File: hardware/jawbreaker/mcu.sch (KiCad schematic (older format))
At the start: 114 parts, among them J1 GSG-USB-MICRO-B, P1 ANALOG, P10 BANK1_AUX, P11 SPIFI, P12 SD, P13 ADC/DAC, P14 LPC_ISP, P15 I2S, P16 1V8, P17 VCC, P18 CPLD_JTAG, P19 BOOT1, P2 LPC_JTAG, P20 BOOT2, P21 BOOT3, P22 BANK1_PWR, P3 LPC_MISC, P4 BOOT0, P5 GPIO, P6 CLOCK_CTL, P7 XCVR_CTL, P8 BANK2_AUX, P9 SPI, U1 GSG-IP4220CZ6, U2 LPC43XXFBD144, U3 W25Q80BV, U4 GSG-XC2C64A-7VQG100C, U5 TPS62410

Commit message: dedicated crystal for mcu. also GP_CLKIN from clock generator as an option
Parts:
- added C? (x2): 10pF, symbol C
- added X?: MCU_XTAL, symbol GSG-XTAL4PIN
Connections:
- net GND: now also C?.2, C?.2, X?.2, X?.4
- net XTAL1: now also C?.1, X?.1; no longer C16.2, C18.2
- net XTAL2: now reaches U2.13 (XTAL2)
- net XTAL2: now also C?.1, X?.3
- net GP_CLKIN: now reaches U2.14 (P4_7)
- net GP_CLKIN: now also C16.2, C18.2
- no-connect marks 32 -> 30
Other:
- moved on the sheet: P10, P7, P8

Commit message: changed boot jumper headers to resistors
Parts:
- removed P19: BOOT1, symbol CONN_3
- removed P20: BOOT2, symbol CONN_3
- removed P21: BOOT3, symbol CONN_3
- removed P4: BOOT0, symbol CONN_3
- added R? (x4): DNP, symbol R
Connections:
- net BOOT0: now also R?.2
- net BOOT1: now also R41.2, R?.1; no longer R41.1
- net BOOT2: now also R42.2, R?.1; no longer R42.1
- net BOOT3: now also R43.2, R?.1; no longer R43.1
- net GND: now also R41.1, R42.1, R43.1, R?.1
- net VCC: now also R4.2, R?.2, R?.2, R?.2
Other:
- moved on the sheet: C?, R4, R41, R42, R43, X?

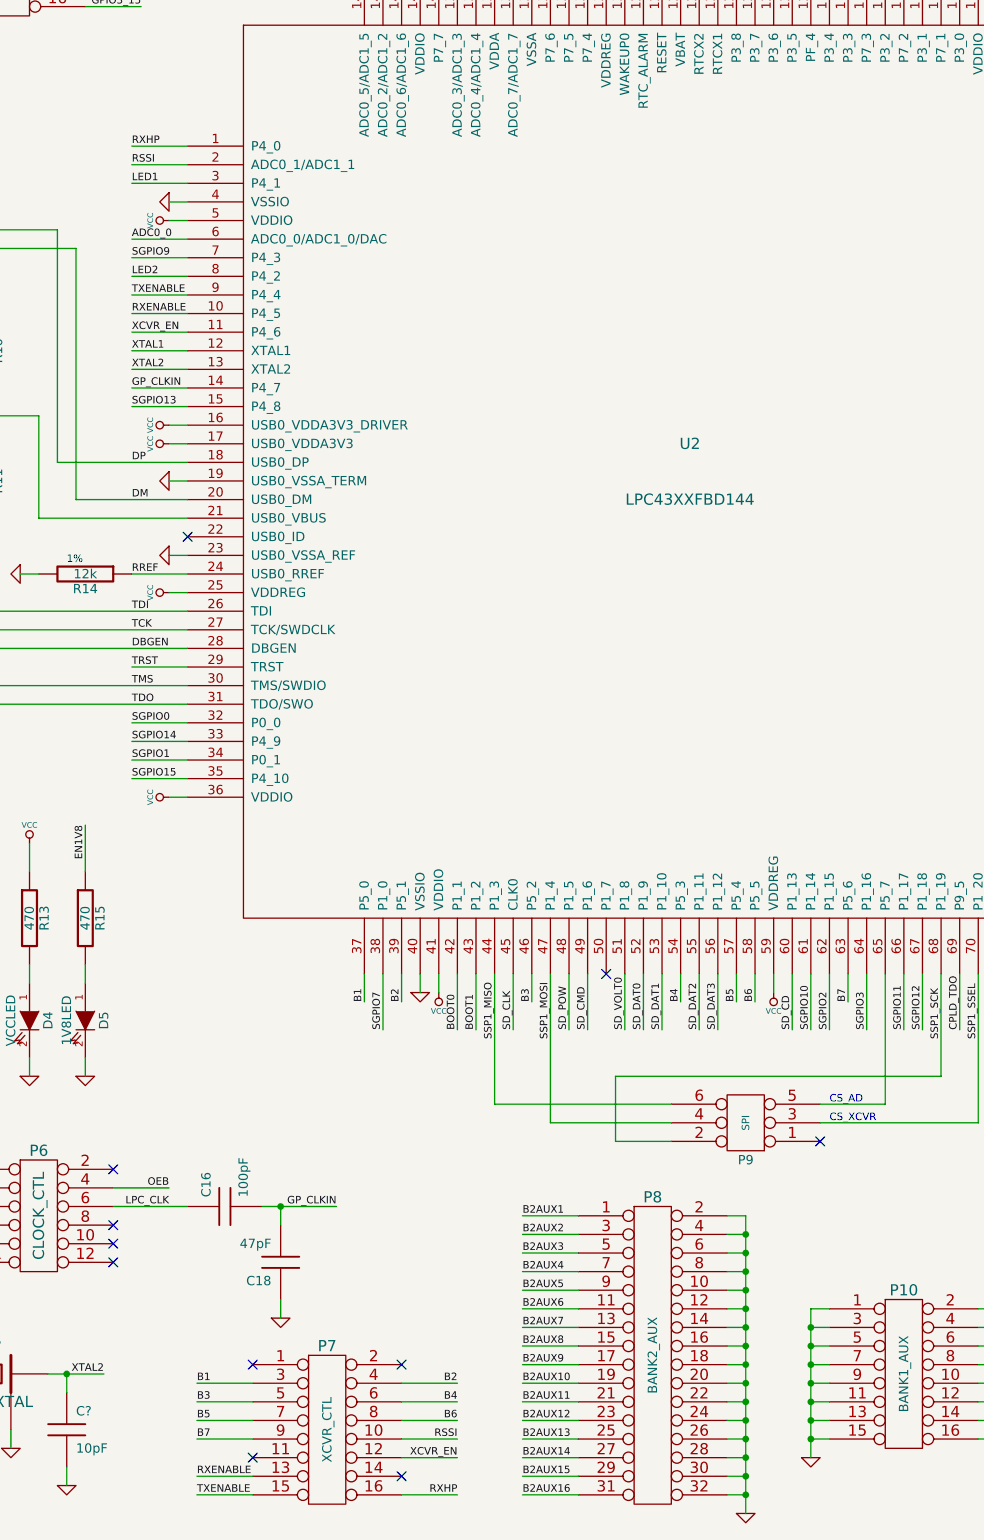
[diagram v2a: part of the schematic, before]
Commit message: removed XCVR_CTL signals that we never used
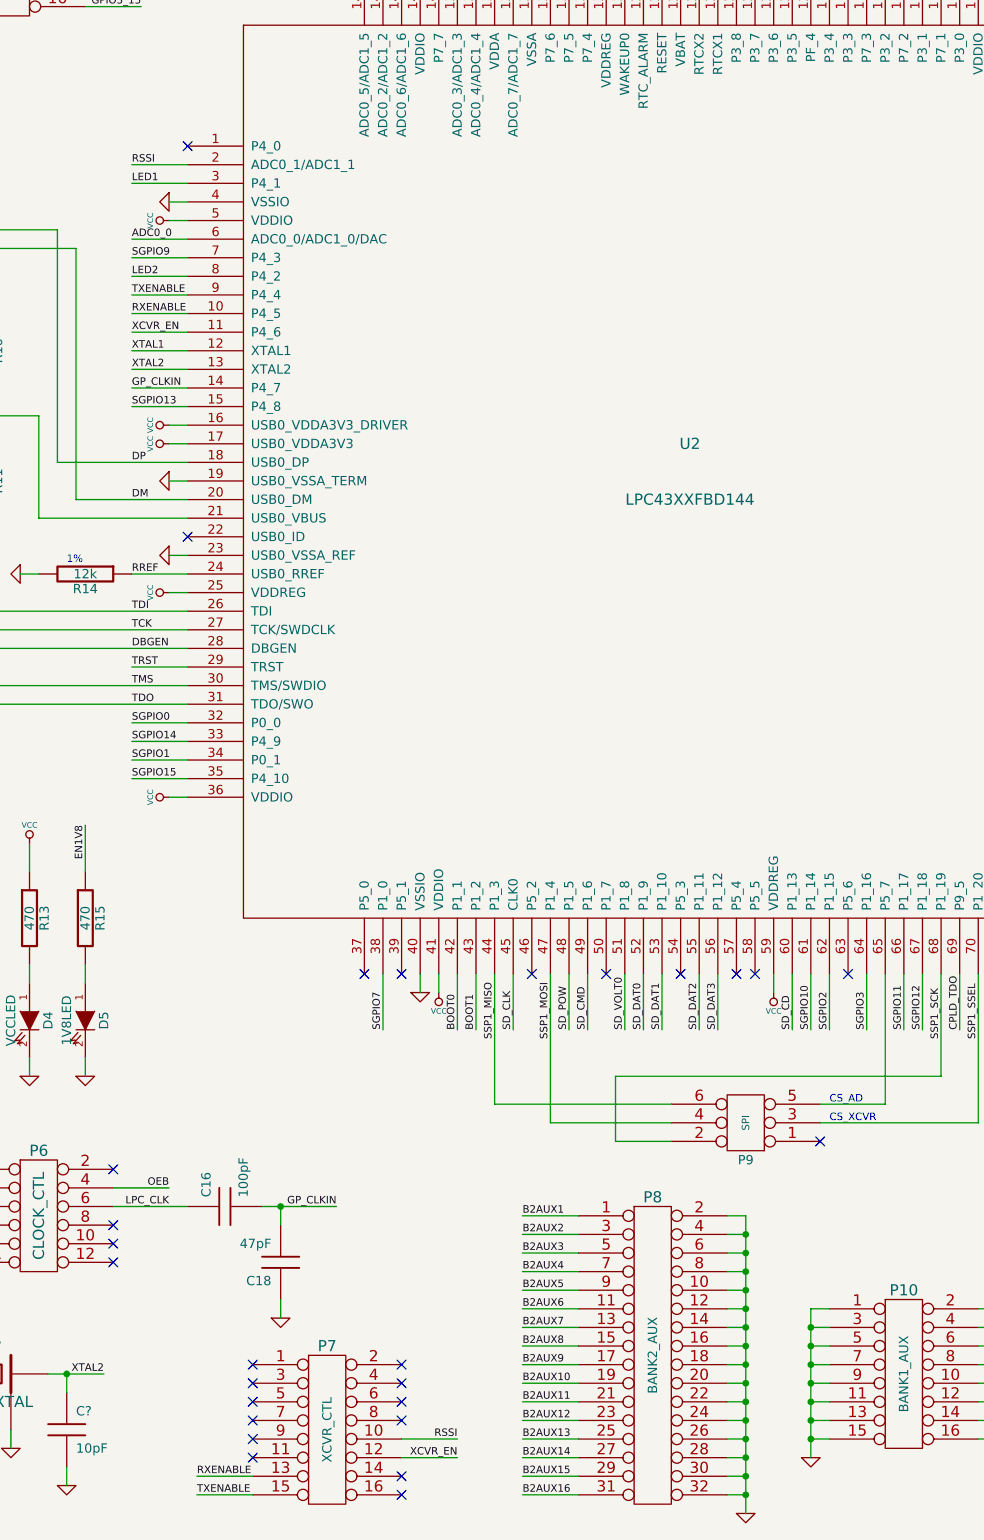
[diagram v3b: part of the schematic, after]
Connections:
- net B1: no longer names the net of U2.37 (P5_0)
- net B1: no longer P7.3
- net B2: no longer names the net of U2.39 (P5_1)
- net B2: no longer P7.4
- net B3: no longer names the net of U2.46 (P5_2)
- net B3: no longer P7.5
- net B4: no longer names the net of U2.54 (P5_3)
- net B4: no longer P7.6
- net B5: no longer names the net of U2.57 (P5_4)
- net B5: no longer P7.7
- net B6: no longer names the net of U2.58 (P5_5)
- net B6: no longer P7.8
- net B7: no longer names the net of U2.63 (P5_6)
- net B7: no longer P7.9
- net RXHP: no longer names the net of U2.1 (P4_0)
- net RXHP: no longer P7.16
- no-connect marks 30 -> 46
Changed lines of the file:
@@
-EESchema Schematic File Version 2  date Thu Aug 23 23:42:08 2012
+EESchema Schematic File Version 2  date Thu Aug 23 23:50:26 2012
 LIBS:power
 LIBS:device
@@
 Comment4 ""
 $EndDescr
-Text Label 2300 9300 2    40   ~ 0
-BOOT3
-$Comp
-L VCC #PWR?
-U 1 1 503713EC
-P 2050 8600
-F 0 "#PWR?" H 2050 8700 30  0001 C CNN
-F 1 "VCC" H 2050 8700 30  0000 C CNN
-	1    2050 8600
-	1    0    0    -1
-$EndComp
-$Comp
-L R R?
-U 1 1 503713EB
-P 2050 8950
-F 0 "R?" V 2130 8950 50  0000 C CNN
-F 1 "DNP" V 2050 8950 50  0000 C CNN
-F 4 "Panasonic" H 2050 8950 60  0001 C CNN "Manufacturer"
-F 5 "ERJ-3GEYJ103V" H 2050 8950 60  0001 C CNN "Part Number"
-F 6 "RES 10K OHM 1/10W 5% 0603 SMD" H 2050 8950 60  0001 C CNN "Description"
-	1    2050 8950
-	-1   0    0    1
-$EndComp
-$Comp
-L GND #PWR?
-U 1 1 503713EA
-P 2050 10000
-F 0 "#PWR?" H 2050 10000 30  0001 C CNN
-F 1 "GND" H 2050 9930 30  0001 C CNN
-	1    2050 10000
-	1    0    0    -1
-$EndComp
+NoConn ~ 7850 7450
+NoConn ~ 7350 7450
+NoConn ~ 7250 7450
+NoConn ~ 6950 7450
+NoConn ~ 6150 7450
+NoConn ~ 5450 7450
+NoConn ~ 5250 7450
 Wire Wire Line
 	2050 10000 2050 9900
@@
 Wire Wire Line
 	1600 10000 1600 9900
-$Comp
-L GND #PWR?
-U 1 1 503713B9
-P 1600 10000
-F 0 "#PWR?" H 1600 10000 30  0001 C CNN
-F 1 "GND" H 1600 9930 30  0001 C CNN
-	1    1600 10000
-	1    0    0    -1
-$EndComp
-$Comp
-L R R?
-U 1 1 503713B8
-P 1600 8950
-F 0 "R?" V 1680 8950 50  0000 C CNN
-F 1 "DNP" V 1600 8950 50  0000 C CNN
-F 4 "Panasonic" H 1600 8950 60  0001 C CNN "Manufacturer"
-F 5 "ERJ-3GEYJ103V" H 1600 8950 60  0001 C CNN "Part Number"
-F 6 "RES 10K OHM 1/10W 5% 0603 SMD" H 1600 8950 60  0001 C CNN "Description"
-	1    1600 8950
-	-1   0    0    1
-$EndComp
-$Comp
-L VCC #PWR?
-U 1 1 503713B7
-P 1600 8600
-F 0 "#PWR?" H 1600 8700 30  0001 C CNN
-F 1 "VCC" H 1600 8700 30  0000 C CNN
-	1    1600 8600
-	1    0    0    -1
-$EndComp
-Text Label 1850 9300 2    40   ~ 0
-BOOT2
-Text Label 1400 9300 2    40   ~ 0
-BOOT1
-$Comp
-L VCC #PWR?
-U 1 1 50371392
-P 1150 8600
-F 0 "#PWR?" H 1150 8700 30  0001 C CNN
-F 1 "VCC" H 1150 8700 30  0000 C CNN
-	1    1150 8600
-	1    0    0    -1
-$EndComp
-$Comp
-L R R?
-U 1 1 50371390
-P 1150 8950
-F 0 "R?" V 1230 8950 50  0000 C CNN
-F 1 "DNP" V 1150 8950 50  0000 C CNN
-F 4 "Panasonic" H 1150 8950 60  0001 C CNN "Manufacturer"
-F 5 "ERJ-3GEYJ103V" H 1150 8950 60  0001 C CNN "Part Number"
-F 6 "RES 10K OHM 1/10W 5% 0603 SMD" H 1150 8950 60  0001 C CNN "Description"
-	1    1150 8950
-	-1   0    0    1
-$EndComp
-$Comp
-L GND #PWR?
-U 1 1 5037138F
-P 1150 10000
-F 0 "#PWR?" H 1150 10000 30  0001 C CNN
-F 1 "GND" H 1150 9930 30  0001 C CNN
-	1    1150 10000
-	1    0    0    -1
-$EndComp
 Wire Wire Line
 	1150 10000 1150 9900
@@
 	5450 9950 5750 9950
 Wire Wire Line
-	5450 9750 5750 9750
-Wire Wire Line
 	4650 10250 4350 10250
 Wire Wire Line
-	4650 9850 4350 9850
-Wire Wire Line
-	4650 9650 4350 9650
-Wire Wire Line
-	7350 7450 7350 7600
-Wire Wire Line
-	6950 7450 6950 7600
-Wire Wire Line
-	6150 7450 6150 7600
-Wire Wire Line
-	5250 7450 5250 7600
-Wire Wire Line
 	16150 2250 16150 2150
 Wire Wire Line
@@
 	16150 1650 16150 1550
 Wire Wire Line
-	5450 7450 5450 7600
-Wire Wire Line
-	7250 7450 7250 7600
-Wire Wire Line
-	7850 7450 7850 7600
-Wire Wire Line
-	4650 9750 4350 9750
-Wire Wire Line
-	4650 9950 4350 9950
-Wire Wire Line
 	4650 10150 4350 10150
 Wire Wire Line
-	5450 9650 5750 9650
-Wire Wire Line
-	5450 9850 5750 9850
-Wire Wire Line
 	5450 10050 5750 10050
 Wire Wire Line
-	5450 10250 5750 10250
-Wire Wire Line
 	4300 3900 4000 3900
 Wire Wire Line
-	4300 3000 4000 3000
-Wire Wire Line
 	3100 8700 2900 8700
 Wire Wire Line
@@
 Wire Wire Line
 	700  10000 700  9900
+NoConn ~ 4300 3000
+NoConn ~ 5450 10250
+NoConn ~ 5450 9850
+NoConn ~ 5450 9750
+NoConn ~ 5450 9650
+NoConn ~ 4650 9950
+NoConn ~ 4650 9850
+NoConn ~ 4650 9750
+NoConn ~ 4650 9650
+Text Label 2300 9300 2    40   ~ 0
+BOOT3
+$Comp
+L VCC #PWR?
+U 1 1 503713EC
+P 2050 8600
+F 0 "#PWR?" H 2050 8700 30  0001 C CNN
+F 1 "VCC" H 2050 8700 30  0000 C CNN
+	1    2050 8600
+	1    0    0    -1
+$EndComp
+$Comp
+L R R?
+U 1 1 503713EB
+P 2050 8950
+F 0 "R?" V 2130 8950 50  0000 C CNN
+F 1 "DNP" V 2050 8950 50  0000 C CNN
+F 4 "Panasonic" H 2050 8950 60  0001 C CNN "Manufacturer"
+F 5 "ERJ-3GEYJ103V" H 2050 8950 60  0001 C CNN "Part Number"
+F 6 "RES 10K OHM 1/10W 5% 0603 SMD" H 2050 8950 60  0001 C CNN "Description"
+	1    2050 8950
+	-1   0    0    1
+$EndComp
+$Comp
+L GND #PWR?
+U 1 1 503713EA
+P 2050 10000
+F 0 "#PWR?" H 2050 10000 30  0001 C CNN
+F 1 "GND" H 2050 9930 30  0001 C CNN
+	1    2050 10000
+	1    0    0    -1
+$EndComp
+$Comp
+L GND #PWR?
+U 1 1 503713B9
+P 1600 10000
+F 0 "#PWR?" H 1600 10000 30  0001 C CNN
+F 1 "GND" H 1600 9930 30  0001 C CNN
+	1    1600 10000
+	1    0    0    -1
+$EndComp
+$Comp
+L R R?
+U 1 1 503713B8
+P 1600 8950
+F 0 "R?" V 1680 8950 50  0000 C CNN
+F 1 "DNP" V 1600 8950 50  0000 C CNN
+F 4 "Panasonic" H 1600 8950 60  0001 C CNN "Manufacturer"
+F 5 "ERJ-3GEYJ103V" H 1600 8950 60  0001 C CNN "Part Number"
+F 6 "RES 10K OHM 1/10W 5% 0603 SMD" H 1600 8950 60  0001 C CNN "Description"
+	1    1600 8950
+	-1   0    0    1
+$EndComp
+$Comp
+L VCC #PWR?
+U 1 1 503713B7
+P 1600 8600
+F 0 "#PWR?" H 1600 8700 30  0001 C CNN
+F 1 "VCC" H 1600 8700 30  0000 C CNN
+	1    1600 8600
+	1    0    0    -1
+$EndComp
+Text Label 1850 9300 2    40   ~ 0
+BOOT2
+Text Label 1400 9300 2    40   ~ 0
+BOOT1
+$Comp
+L VCC #PWR?
+U 1 1 50371392
+P 1150 8600
+F 0 "#PWR?" H 1150 8700 30  0001 C CNN
+F 1 "VCC" H 1150 8700 30  0000 C CNN
+	1    1150 8600
+	1    0    0    -1
+$EndComp
+$Comp
+L R R?
+U 1 1 50371390
+P 1150 8950
+F 0 "R?" V 1230 8950 50  0000 C CNN
+F 1 "DNP" V 1150 8950 50  0000 C CNN
+F 4 "Panasonic" H 1150 8950 60  0001 C CNN "Manufacturer"
+F 5 "ERJ-3GEYJ103V" H 1150 8950 60  0001 C CNN "Part Number"
+F 6 "RES 10K OHM 1/10W 5% 0603 SMD" H 1150 8950 60  0001 C CNN "Description"
+	1    1150 8950
+	-1   0    0    1
+$EndComp
+$Comp
+L GND #PWR?
+U 1 1 5037138F
+P 1150 10000
+F 0 "#PWR?" H 1150 10000 30  0001 C CNN
+F 1 "GND" H 1150 9930 30  0001 C CNN
+	1    1150 10000
+	1    0    0    -1
+$EndComp
 $Comp
 L GND #PWR?
@@
 	1    0    0    -1
 $EndComp
-Text Label 4000 3000 0    40   ~ 0
-RXHP
 Text Label 4000 3800 0    40   ~ 0
 TXENABLE
@@
 NoConn ~ 4650 10050
 NoConn ~ 5450 10150
-Text Label 5750 10250 2    40   ~ 0
-RXHP
 Text Label 5750 10050 2    40   ~ 0
 XCVR_EN
 Text Label 5750 9950 2    40   ~ 0
 RSSI
-Text Label 5750 9850 2    40   ~ 0
-B6
-Text Label 4350 9950 0    40   ~ 0
-B7
-Text Label 4350 9850 0    40   ~ 0
-B5
-Text Label 4350 9750 0    40   ~ 0
-B3
-Text Label 5750 9750 2    40   ~ 0
-B4
-Text Label 5750 9650 2    40   ~ 0
-B2
-Text Label 4350 9650 0    40   ~ 0
-B1
 Text Label 4350 10150 0    40   ~ 0
 RXENABLE
@@
 	1    0    0    -1
 $EndComp
-Text Label 7850 7600 1    40   ~ 0
-B7
-Text Label 7350 7600 1    40   ~ 0
-B6
-Text Label 7250 7600 1    40   ~ 0
-B5
-Text Label 6950 7600 1    40   ~ 0
-B4
-Text Label 6150 7600 1    40   ~ 0
-B3
-Text Label 5450 7600 1    40   ~ 0
-B2
 NoConn ~ 6550 7450
-Text Label 5250 7600 1    40   ~ 0
-B1
 Text Notes 7750 8150 0    40   ~ 0
 CS_AD

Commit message: changed bank1 power header to resistors, wired spifi header (cut traces to use header)
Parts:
- removed P22: BANK1_PWR, symbol CONN_3
- added R?: DNP, symbol R
- added R?: 10k, symbol R
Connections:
- net +1.8V: now also R?.2
- net SPIFI_CS: now also P11.7 (P7), U3.1 (CS)
- net SPIFI_MISO: now also P11.1 (P1), U3.2 (DO)
- net SPIFI_MOSI: now also P11.3 (P3), U3.5 (DI)
- net SPIFI_SCK: now also P11.5 (P5), U3.6 (CLK)
- net SPIFI_SIO2: now also P11.11, U3.3 (WP)
- net SPIFI_SIO3: now also P11.9, U3.7 (HOLD)
- net VCC: now also R?.2
- net VCCIO1: now also R?.1, R?.1

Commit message: global labels for DA* and DD*, 39 ohm series resistors
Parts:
- removed P13: ADC/DAC, symbol CONN_20X2
- removed R19, R20, R21, R22, R23, R24, R25, R26, R27: 100, symbol R
- added R? (x17): 39, symbol R
- R18: value 100 -> 39; Description RES 100 OHM 1/10W 5% 0603 SMD -> (none); Manufacturer Panasonic -> (none); Part Number ERJ-3GEYJ101V -> (none)
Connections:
- net DA0: now also R?.2; no longer U4.43 (BANK1F4M8)
- net DA1: now also R?.2; no longer U4.42 (BANK1F4M7)
- net DA2: now also R?.2; no longer U4.41 (BANK1F4M6)
- net DA3: now also R?.2; no longer U4.40 (BANK1F4M5)
- net DA4: now also R?.2; no longer U4.39 (BANK1F4M4)
- net DA5: now also R?.2; no longer U4.37 (BANK1F4M3)
- net DA6: now also R?.2; no longer U4.36 (BANK1F4M2)
- net DA7: now also R?.2; no longer U4.35 (BANK1F4M1)
- net DD0: now also R?.2; no longer U4.34 (BANK1F2M16)
- net DD1: now also R?.2; no longer U4.33 (BANK1F2M15)
- net DD2: now also R?.2; no longer U4.32 (BANK1F2M14)
- net DD3: now also R?.2; no longer U4.30 (BANK1F2M13)
- net DD4: now also R?.2; no longer U4.29 (BANK1F2M12)
- net DD5: now also R?.2; no longer U4.28 (BANK1F2M11)
- net DD6: now also R?.2; no longer U4.24 (BANK1F2M9)
- net DD7: now also R?.2; no longer U4.19 (BANK1F2M6)
- net DD8: now also R?.2; no longer U4.18 (BANK1F2M5)
- net DD9: now also R18.2; no longer R18.1, U4.17 (BANK1F2M4)
- new net BANK1F2M11: R?.1, U4.28 (BANK1F2M11)
- new net BANK1F2M12: R?.1, U4.29 (BANK1F2M12)
- new net BANK1F2M13: R?.1, U4.30 (BANK1F2M13)
- new net BANK1F2M14: R?.1, U4.32 (BANK1F2M14)
- new net BANK1F2M15: R?.1, U4.33 (BANK1F2M15)
- new net BANK1F2M16: R?.1, U4.34 (BANK1F2M16)
- new net BANK1F2M4: R18.1, U4.17 (BANK1F2M4)
- new net BANK1F2M5: R?.1, U4.18 (BANK1F2M5)
- new net BANK1F2M6: R?.1, U4.19 (BANK1F2M6)
- new net BANK1F2M9: R?.1, U4.24 (BANK1F2M9)
- new net BANK1F4M1: R?.1, U4.35 (BANK1F4M1)
- new net BANK1F4M2: R?.1, U4.36 (BANK1F4M2)
- new net BANK1F4M3: R?.1, U4.37 (BANK1F4M3)
- new net BANK1F4M4: R?.1, U4.39 (BANK1F4M4)
- new net BANK1F4M5: R?.1, U4.40 (BANK1F4M5)
- new net BANK1F4M6: R?.1, U4.41 (BANK1F4M6)
- new net BANK1F4M7: R?.1, U4.42 (BANK1F4M7)
- new net BANK1F4M8: R?.1, U4.43 (BANK1F4M8)
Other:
- moved on the sheet: R18

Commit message: global labels for xcvr control
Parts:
- removed P7: XCVR_CTL, symbol CONN_8X2
- P11: Note (none) -> DNP
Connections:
- no-connect marks 46 -> 34
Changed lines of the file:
@@
-EESchema Schematic File Version 2  date Fri Aug 24 00:37:44 2012
+EESchema Schematic File Version 2  date Fri Aug 24 09:40:20 2012
 LIBS:power
 LIBS:device
@@
 Comment4 ""
 $EndDescr
+Text GLabel 4200 4000 0    40   Input ~ 0
+XCVR_EN
+Text GLabel 4200 3900 0    40   Input ~ 0
+RXENABLE
+Text GLabel 4200 3800 0    40   Input ~ 0
+TXENABLE
+Text GLabel 4200 3100 0    40   Input ~ 0
+RSSI
 Text GLabel 11400 7850 0    40   Input ~ 0
 GCK0
@@
 	8350 2050 8350 1750
 Wire Wire Line
-	4300 3100 4000 3100
+	4300 3100 4200 3100
 Wire Wire Line
 	9550 7400 9900 7400
@@
 	3100 8600 2900 8600
 Wire Wire Line
-	4300 3800 4000 3800
-Wire Wire Line
-	4300 4000 4000 4000
+	4300 3800 4200 3800
 Wire Wire Line
-	5450 9950 5750 9950
-Wire Wire Line
-	4650 10250 4350 10250
+	4300 4000 4200 4000
 Wire Wire Line
 	16150 2250 16150 2150
@@
 	16150 1650 16150 1550
 Wire Wire Line
-	4650 10150 4350 10150
-Wire Wire Line
-	5450 10050 5750 10050
-Wire Wire Line
-	4300 3900 4000 3900
+	4300 3900 4200 3900
 Wire Wire Line
 	3100 8700 2900 8700
@@
 NoConn ~ 5250 7450
 NoConn ~ 4300 3000
-NoConn ~ 5450 10250
-NoConn ~ 5450 9850
-NoConn ~ 5450 9750
-NoConn ~ 5450 9650
-NoConn ~ 4650 9950
-NoConn ~ 4650 9850
-NoConn ~ 4650 9750
-NoConn ~ 4650 9650
 Text Label 2300 9300 2    40   ~ 0
 BOOT3
@@
 Text Label 8650 1750 3    40   ~ 0
 GPIO3_8
-Text Label 4000 3100 0    40   ~ 0
-RSSI
 $Comp
 L VCC #PWR026
@@
 	1    0    0    -1
 $EndComp
-Text Label 4000 3800 0    40   ~ 0
-TXENABLE
-Text Label 4000 3900 0    40   ~ 0
-RXENABLE
-Text Label 4000 4000 0    40   ~ 0
-XCVR_EN
-NoConn ~ 4650 9550
-NoConn ~ 5450 9550
-NoConn ~ 4650 10050
-NoConn ~ 5450 10150
-Text Label 5750 10050 2    40   ~ 0
-XCVR_EN
-Text Label 5750 9950 2    40   ~ 0
-RSSI
-Text Label 4350 10150 0    40   ~ 0
-RXENABLE
-Text Label 4350 10250 0    40   ~ 0
-TXENABLE
-$Comp
-L CONN_8X2 P7
-U 1 1 4F836FF2
-P 5050 9900
-F 0 "P7" H 5050 10350 60  0000 C CNN
-F 1 "XCVR_CTL" V 5050 9900 50  0000 C CNN
-	1    5050 9900
-	1    0    0    -1
-$EndComp
 NoConn ~ 6550 7450
 Text Notes 7750 8150 0    40   ~ 0
@@
 F 0 "P11" H 8650 1300 60  0000 C CNN
 F 1 "SPIFI" V 8650 950 60  0000 C CNN
+F 4 "DNP" H 8650 600 60  0000 C CNN "Note"
 	1    8650 950
 	-1   0    0    1
